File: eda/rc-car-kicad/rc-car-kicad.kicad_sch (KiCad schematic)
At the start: 55 parts, among them Q1 MMBT3904, Q2 IRLML2246, Q3 IRLML2246, Q4 MMBT3904, Q5 IRLML6244, Q6 IRLML6244, SW1 SW_SPST, U1 TPS3840, U2 MIC3975-5.0YMM, U3 MIC5225-3.3YM5, U4 ATmega164A-A

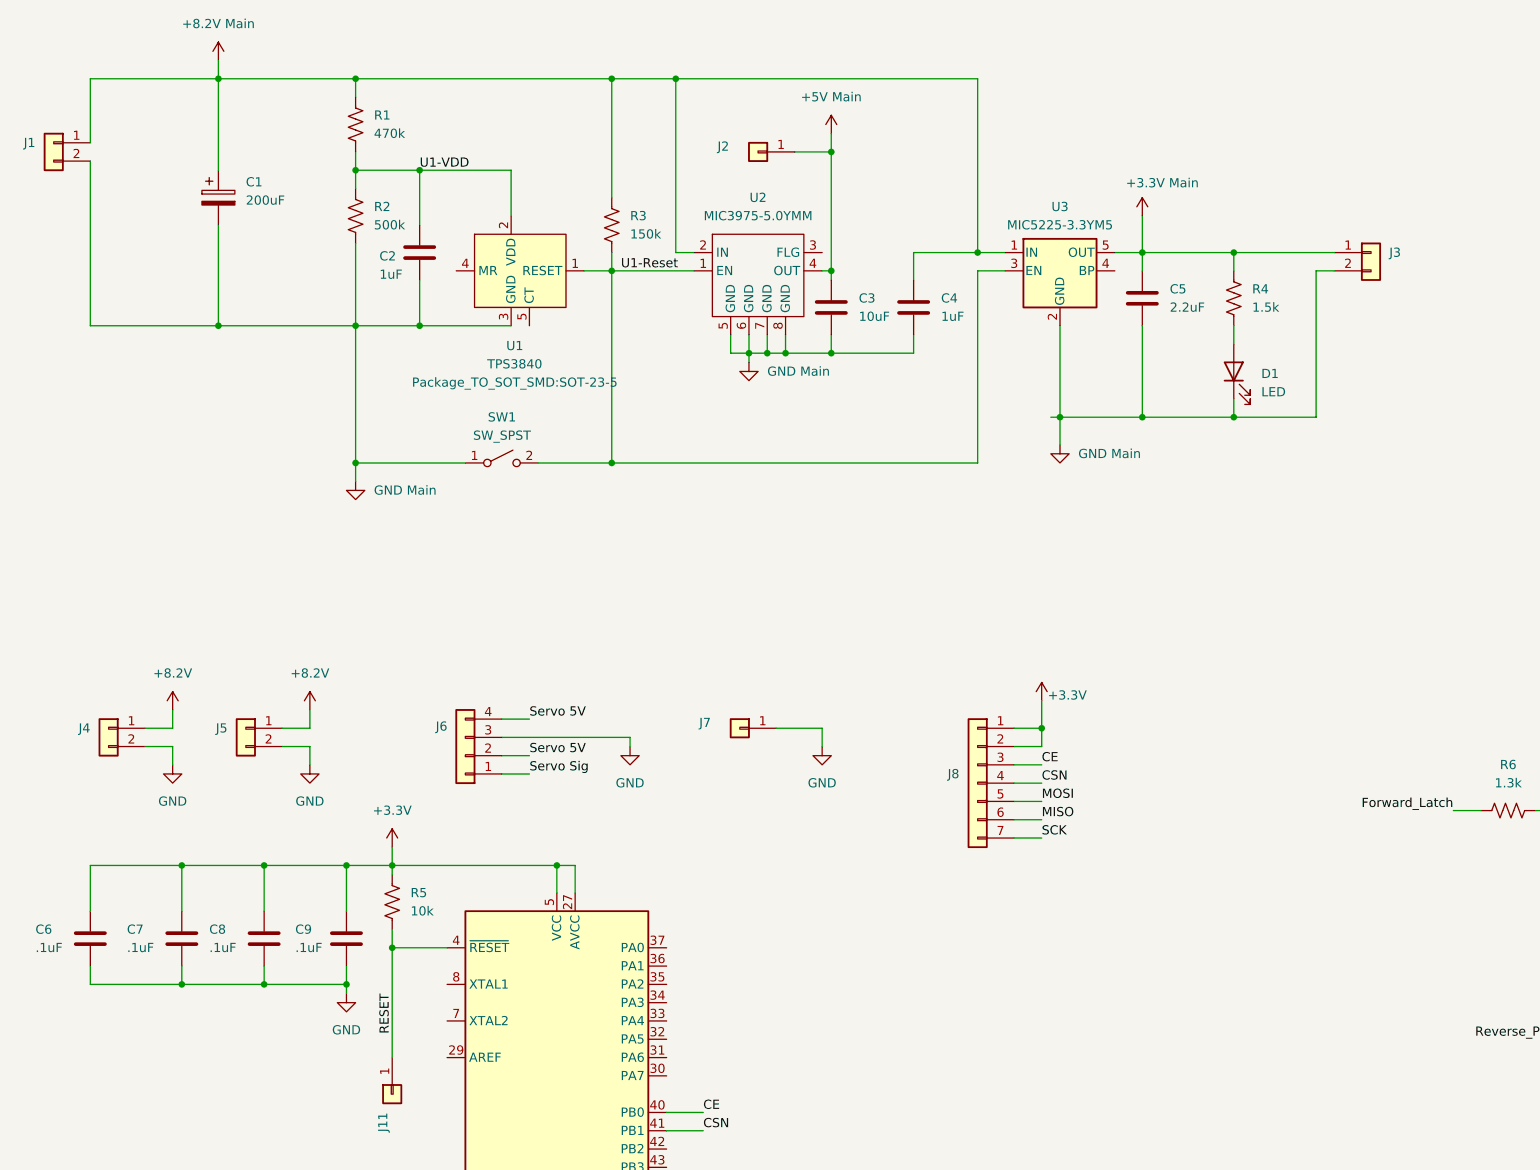
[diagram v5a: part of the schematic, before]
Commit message: - Modified the header pins a bit on the pcb
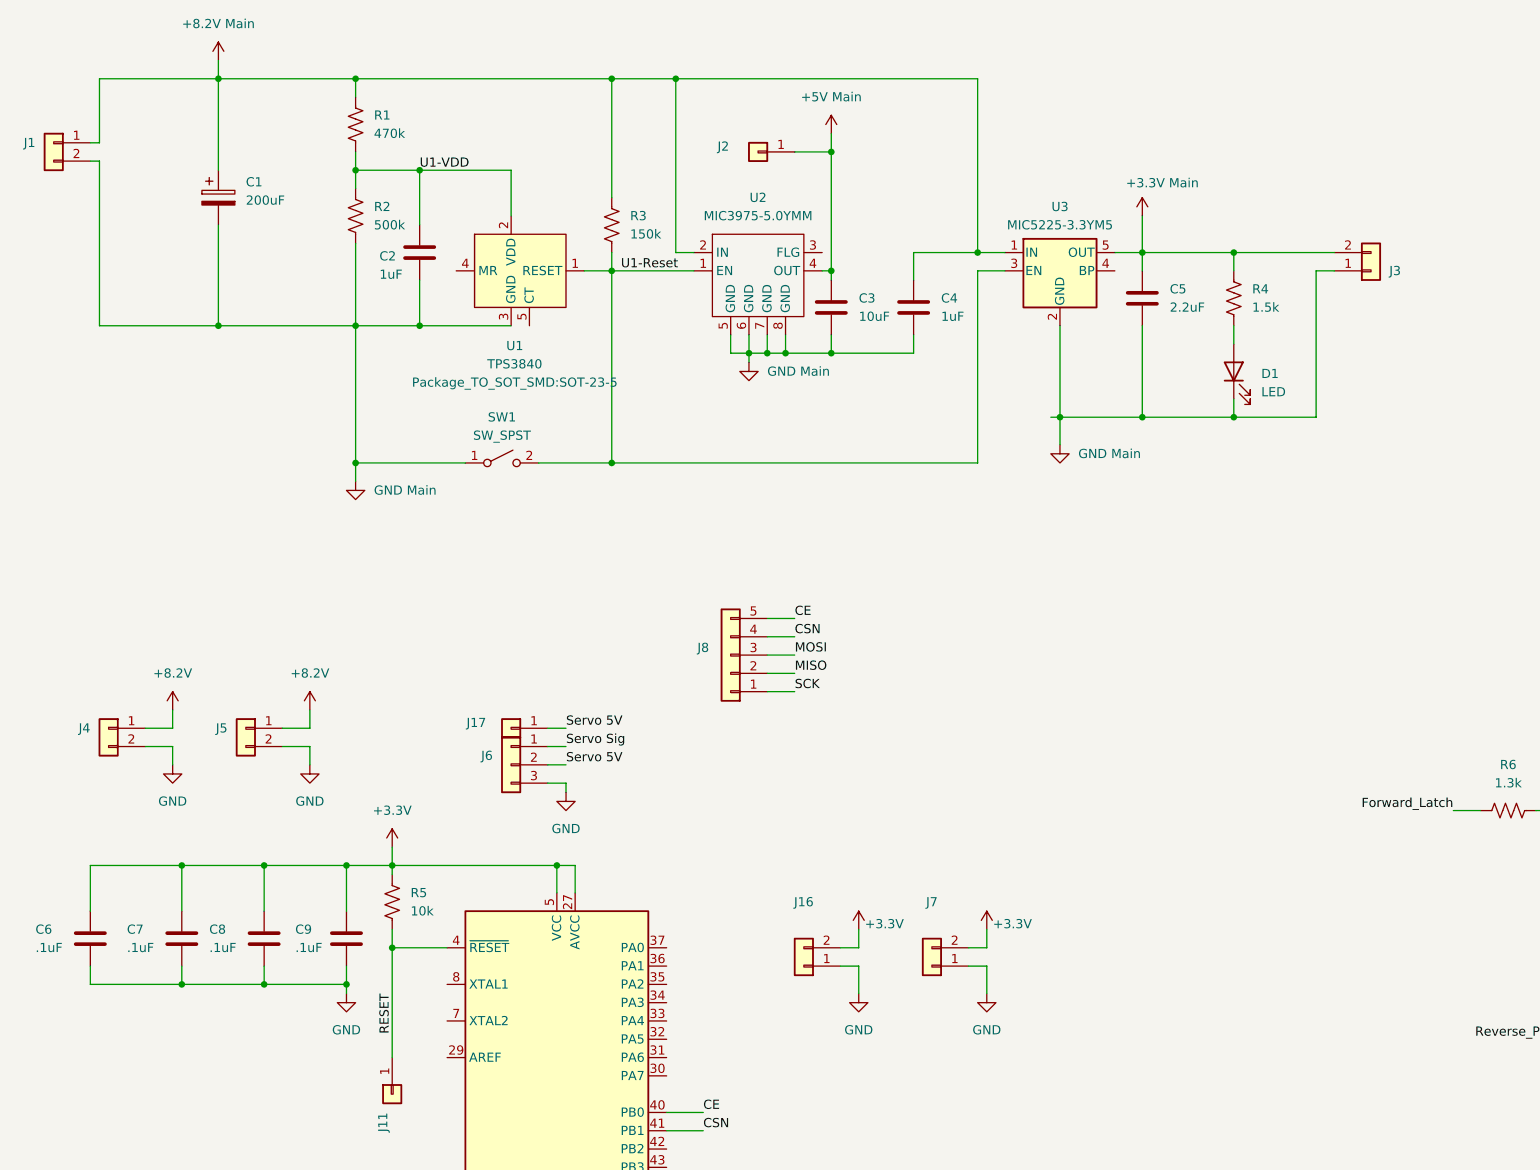
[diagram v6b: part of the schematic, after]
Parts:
- removed J6: ~, Connector_PinHeader_2.54mm:PinHeader_1x04_P2.54mm_Vertical, symbol Connector_Generic:Conn_01x04
- removed J7: ~, Connector_PinHeader_2.54mm:PinHeader_1x01_P2.54mm_Vertical, symbol Connector_Generic:Conn_01x01
- removed J8: ~, Connector_PinHeader_2.54mm:PinHeader_1x07_P2.54mm_Vertical, symbol Connector_Generic:Conn_01x07
- added J16, J7: ~, _global-libraries:PinHeader_1x02_P2.54mm_Vertical_No_Courtyard, symbol Connector_Generic:Conn_01x02
- added J17: ~, Connector_PinHeader_2.54mm:PinHeader_1x01_P2.54mm_Vertical, symbol Connector_Generic:Conn_01x01
- added J6: ~, Connector_PinHeader_2.54mm:PinHeader_1x03_P2.54mm_Vertical, symbol Connector_Generic:Conn_01x03
- added J8: ~, Connector_PinHeader_2.54mm:PinHeader_1x05_P2.54mm_Vertical, symbol Connector_Generic:Conn_01x05
- J12, J13, J14, J15: value (none) -> ~
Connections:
- net +3.3V: now also J16.2 (Pin_2), J7.2 (Pin_2)
- net +3.3V Main: now also J3.2 (Pin_2); no longer J3.1 (Pin_1)
- net CE: now also J8.5 (Pin_5)
- net CSN: now also J8.4 (Pin_4)
- net GND: now also J16.1 (Pin_1), J6.3 (Pin_3), J7.1 (Pin_1)
- net GND Main: now also J3.1 (Pin_1); no longer J3.2 (Pin_2)
- net MISO: now also J8.2 (Pin_2)
- net MOSI: now also J8.3 (Pin_3)
- net SCK: now also J8.1 (Pin_1)
- net Servo 5V: now also J17.1 (Pin_1), J6.2 (Pin_2)
- net Servo Sig: now also J6.1 (Pin_1)

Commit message: - Documented the schematic and created a pdf of the schematic
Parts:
- C1: footprint Capacitor_THT:CP_Radial_D8.0mm_P3.50mm -> Capacitor_THT:CP_Radial_D6.3mm_P2.50mm
- renumbered J9 to M+, J10 to M-
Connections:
- net +8.2V renamed +8.4V
- net +8.2V Main renamed +8.4V Main
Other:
- note added: "3.3V Headers"
- note added: "8.4V Headers"
- note added: "ATmega164A Control Unit (Board 2)"
- note added: "H-Bridge Motor Driver (Board 2)"
- note added: "Power Management & Regulation (Board 1)"
- note added: "Servo Motor Headers"
- note added: "Test Point"
- note added: "Test Points"
- note added: "nRF24L01+ Headers"
- title: (none) -> RC Car Controller
- moved on the sheet: C1, C2, C3, C4, C5, C6, C7, C8, C9, D1, D2, D3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

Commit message: - Added an images directory with images of the pcb and the schematic - Added a revision number to the pcb. - Finalized pcb and schematic
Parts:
- renumbered M+ to M+1, M- to M-1
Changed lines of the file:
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@@
 		(title "RC Car Controller")
 		(date "2025-09-09")
-		(rev "A")
+		(rev "A1")
 	)
 	(junction
@@
 		(on_board yes)
 		(dnp no)
-		(property "Reference" "M-"
+		(property "Reference" "M-1"
 			(at 328.676 73.66 0)
 			(effects
@@
 			(project "rc-car-kicad"
 				(path "/8c74a705-6515-4bfe-a511-932ab8fcaec8"
-					(reference "M-")
+					(reference "M-1")
 					(unit 1)
 				)
@@
 		(on_board yes)
 		(dnp no)
-		(property "Reference" "M+"
+		(property "Reference" "M+1"
 			(at 314.96 73.406 0)
 			(effects
@@
 			(project "rc-car-kicad"
 				(path "/8c74a705-6515-4bfe-a511-932ab8fcaec8"
-					(reference "M+")
+					(reference "M+1")
 					(unit 1)
 				)
